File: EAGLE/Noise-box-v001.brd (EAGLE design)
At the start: 80.5 x 52.1 mm, 93 parts, among them J1 AVR_SPI_PROG_3X22X3_LOCK, J4 MICRO-SD_CARD_SOCKET, J5 HEADPHONE, J6 POWER_JACK, U1 ATMEGA328P_TQFP, U2 MIC5219 3.3V, U3 MCP73831, Y1 12.288MHz, Y2 8MHz

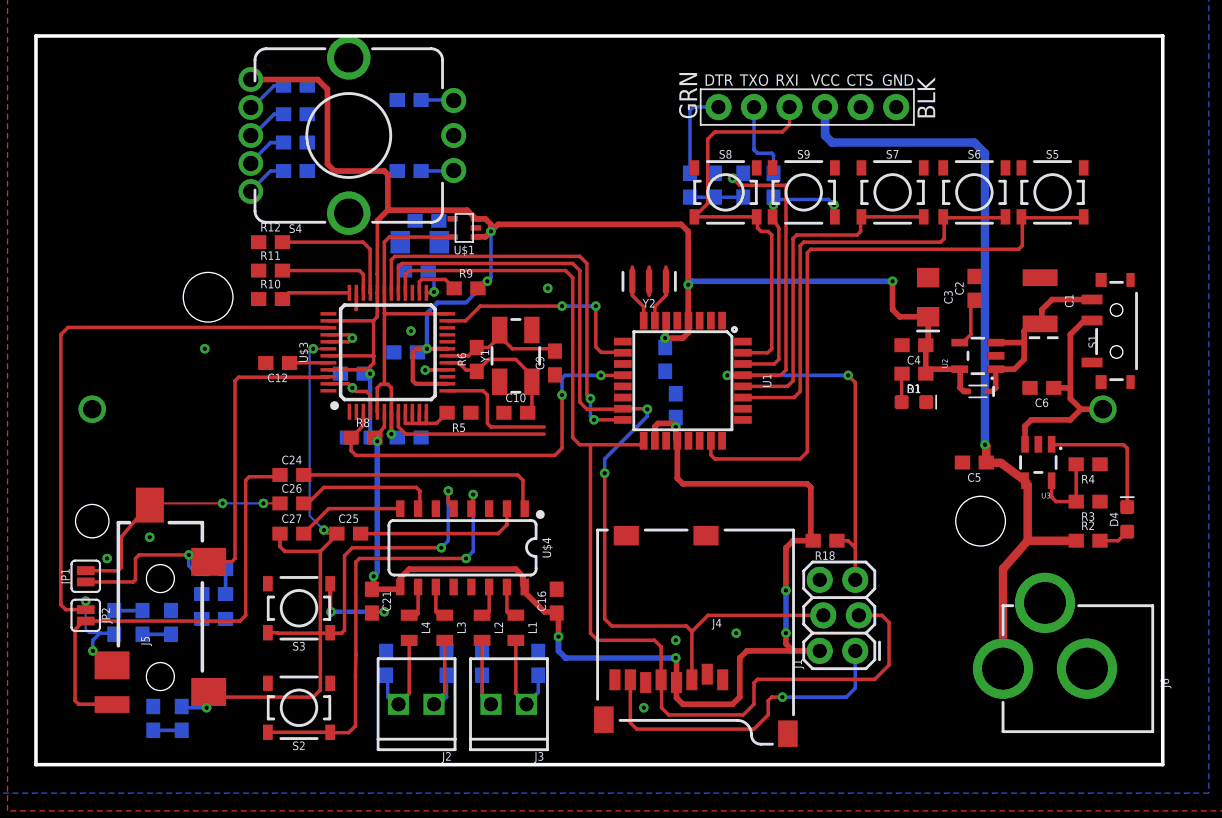
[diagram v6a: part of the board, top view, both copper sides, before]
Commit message: Readme update
Added a bit of formatting. Continued the explanation of the project.
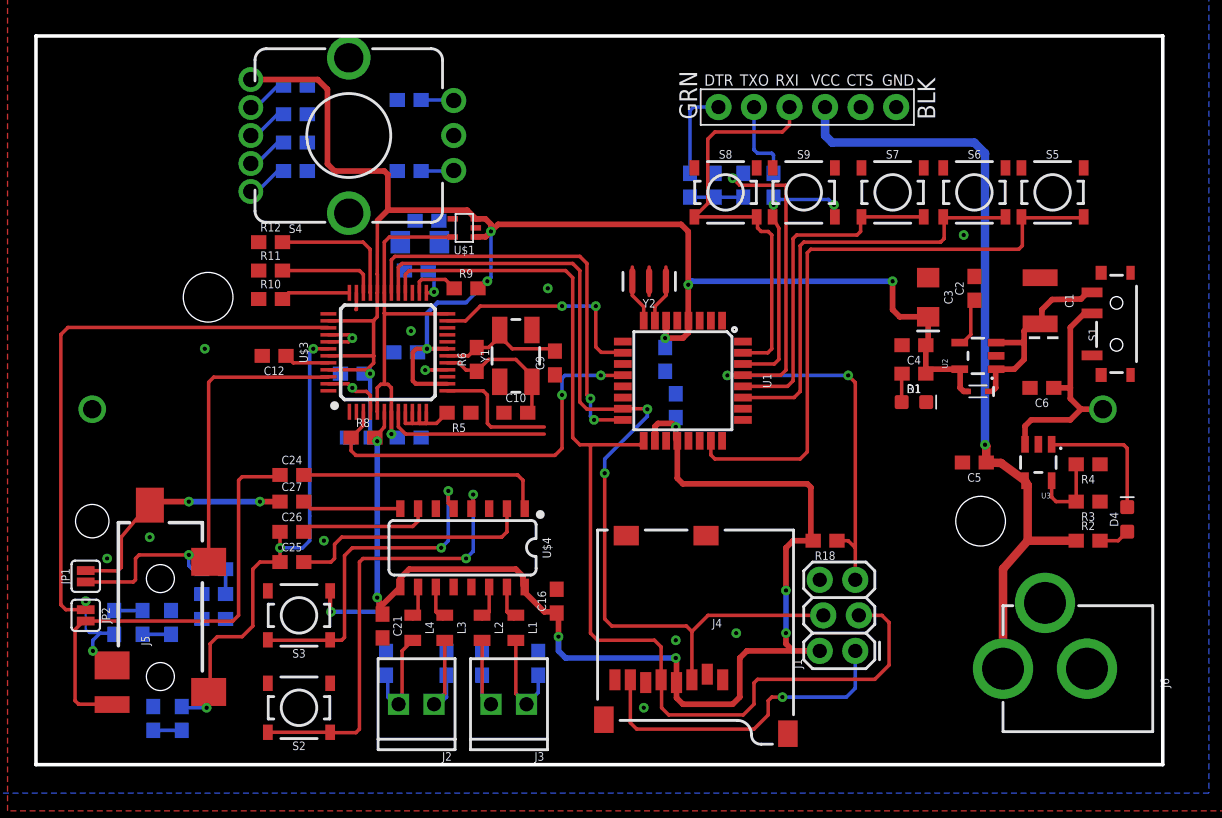
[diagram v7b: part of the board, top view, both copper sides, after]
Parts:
- moved C25 4.54 mm to (16.3, 17.0)
- moved C27 2.29 mm to (16.3, 21.3)
- moved C26 2.03 mm to (16.3, 19.2)
- moved C21 1.93 mm to (22.7, 12.4)
- moved C12 0.57 mm to (15.0, 31.8)
- moved S1 0.51 mm to (75.2, 34.0)
- moved S3 0.51 mm to (16.8, 13.2)
- moved L4 0.25 mm to (24.9, 12.3)
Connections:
- removed net N$28: R22.2, S4.3
- net AMP-L: now also C27.1; no longer C26.1
- net GBUF: now also C26.1; no longer C27.1
- net ROT-SW: now also R22.2, S4.3
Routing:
- net GBUF: track 42.6 -> 35.7 mm
- net N$34: track 11.9 -> 17.7 mm
- net ROT-SW: track 0.00 -> 2.97 mm
- net N$28: track 2.97 -> 0.00 mm
- net +3V3: track 215.5 -> 217.5 mm
- net GND: track 17.7 -> 16.3 mm, vias 13 -> 14
- net N$35: track 10.2 -> 9.38 mm
- net N$42: track 7.64 -> 7.10 mm
- net VBATT: track 16.2 -> 16.7 mm
- net N$43: track 23.8 -> 24.3 mm

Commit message: Layout
Further layout
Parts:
- moved JP2 15.3 mm to (12.4, 24.0)
- moved JP1 10.4 mm to (7.62, 24.4), turned to 180 degrees
- moved C31 6.35 mm to (31.0, 50.0), turned to 180 degrees
- moved C32 6.35 mm to (31.0, 45.0), turned to 180 degrees
- moved C23 1.37 mm to (43.4, 32.8), turned to 180 degrees
- moved Y2 1.27 mm to (41.8, 38.4)
- moved R20 1.02 mm to (16.5, 46.0)
- moved R21 1.02 mm to (16.5, 43.9)
- moved R19 0.76 mm to (16.5, 50.3)
- moved R22 0.76 mm to (16.5, 48.3)
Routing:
- net ROT-LEDR: track 0.00 -> 47.2 mm, vias 0 -> 1
- net ROT-LEDB: track 0.00 -> 43.8 mm, vias 0 -> 1
- net RIGHT: track 48.7 -> 77.8 mm, vias 2 -> 3
- net SD-CS: track 0.00 -> 24.7 mm, vias 0 -> 4
- net AMP-SHDN: track 7.21 -> 31.5 mm, vias 0 -> 2
- net ROT-SW: track 2.97 -> 27.1 mm, vias 0 -> 1
- net ROT-LEDG: track 0.00 -> 21.3 mm
- net MISO: track 53.9 -> 73.5 mm, vias 3 -> 4
- net MP3-DREQ: track 11.7 -> 28.6 mm, vias 0 -> 2
- net ROT-B: track 2.35 -> 15.3 mm, vias 0 -> 1
- net MP3-DCS: track 9.19 -> 18.7 mm, vias 0 -> 2
- net LEFT: track 34.0 -> 27.2 mm
- net MOSI: track 65.8 -> 59.2 mm
- net ROT-A: track 2.35 -> 6.46 mm, vias 0 -> 1
- net +3V3: track 217.5 -> 213.5 mm, vias 14 -> 13
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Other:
- board size 80.5 x 52.1 mm -> 81.3 x 53.3 mm
